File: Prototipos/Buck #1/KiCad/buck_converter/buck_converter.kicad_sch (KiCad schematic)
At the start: 6 parts, among them J1 Screw_Terminal_01x02, J2 Screw_Terminal_01x02, Q2 IRF9540NPBF

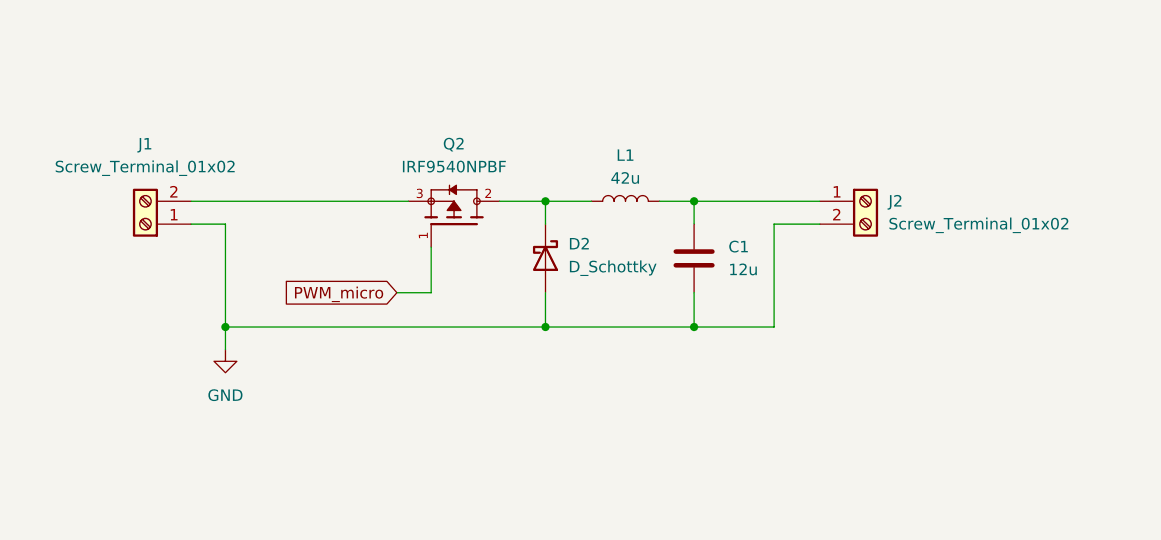
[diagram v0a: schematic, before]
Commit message: Avances circuito KiCad, nuevos calculos para frecuencia más baja
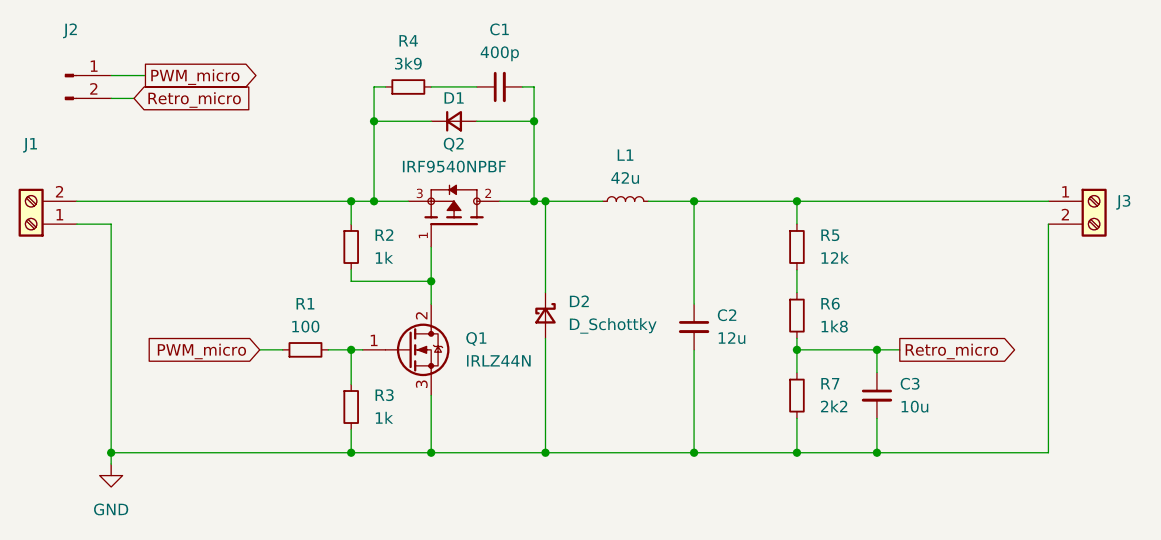
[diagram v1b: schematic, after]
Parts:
- removed C1: 12u, symbol Device:C
- removed D2: D_Schottky, symbol Device:D_Schottky
- removed L1: 42u, symbol Device:L
- added C1: 400p, Capacitor_THT:C_Disc_D3.8mm_W2.6mm_P2.50mm, symbol Device:C_Small
- added C2: 12u, Capacitor_THT:C_Disc_D3.8mm_W2.6mm_P2.50mm, symbol Device:C_Small
- added C3: 10u, Capacitor_THT:C_Disc_D3.8mm_W2.6mm_P2.50mm, symbol Device:C_Small
- added D1: D_Small, Diode_THT:D_A-405_P10.16mm_Horizontal, symbol Device:D_Small
- added D2: D_Schottky, Diode_THT:D_A-405_P10.16mm_Horizontal, symbol Device:D_Schottky_Small
- added J2: Conn_01x02_Pin, Connector_PinHeader_2.54mm:PinHeader_1x02_P2.54mm_Vertical, symbol Connector:Conn_01x02_Pin
- added L1: 42u, Inductor_THT:L_Axial_L16.0mm_D6.3mm_P25.40mm_Horizontal_Fastron_VHBCC, symbol Device:L_Small
- added Q1: IRLZ44N, Package_TO_SOT_THT:TO-220-3_Vertical, symbol Transistor_FET:IRLZ44N
- added R1: 100, Resistor_THT:R_Axial_DIN0207_L6.3mm_D2.5mm_P15.24mm_Horizontal, symbol Device:R_Small
- added R2, R3: 1k, Resistor_THT:R_Axial_DIN0207_L6.3mm_D2.5mm_P15.24mm_Horizontal, symbol Device:R_Small
- added R4: 3k9, Resistor_THT:R_Axial_DIN0207_L6.3mm_D2.5mm_P15.24mm_Horizontal, symbol Device:R_Small
- added R5: 12k, Resistor_THT:R_Axial_DIN0207_L6.3mm_D2.5mm_P15.24mm_Horizontal, symbol Device:R_Small
- added R6: 1k8, Resistor_THT:R_Axial_DIN0207_L6.3mm_D2.5mm_P15.24mm_Horizontal, symbol Device:R_Small
- added R7: 2k2, Resistor_THT:R_Axial_DIN0207_L6.3mm_D2.5mm_P15.24mm_Horizontal, symbol Device:R_Small
- J1: footprint (none) -> TerminalBlock_Phoenix:TerminalBlock_Phoenix_MPT-0,5-2-2.54_1x02_P2.54mm_Horizontal
- J3: renamed from J2; footprint (none) -> TerminalBlock_Phoenix:TerminalBlock_Phoenix_MPT-0,5-2-2.54_1x02_P2.54mm_Horizontal
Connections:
- net GND: now also C2.2, C3.2, D2.2 (A), Q1.3 (S), R3.2, R7.2
- net PWM_micro: now also J2.1 (Pin_1), R1.1; no longer Q2.1
- net at J1.2 (Pin_2), Q2.3: now also D1.1 (K), R2.1, R4.1
- net at Q2.2: now also C1.2, D1.2 (A), D2.1 (K), L1.1
- net at J3.1 (Pin_1): now also C2.1, L1.2, R5.1
- new net: Q1.2 (D), Q2.1, R2.2
- new net: Q1.1 (G), R1.2, R3.1
- new net: C1.1, R4.2
- new net: R5.2, R6.1
- new net Retro_micro: C3.1, J2.2 (Pin_2), R6.2, R7.1
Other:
- moved on the sheet: J1, J3

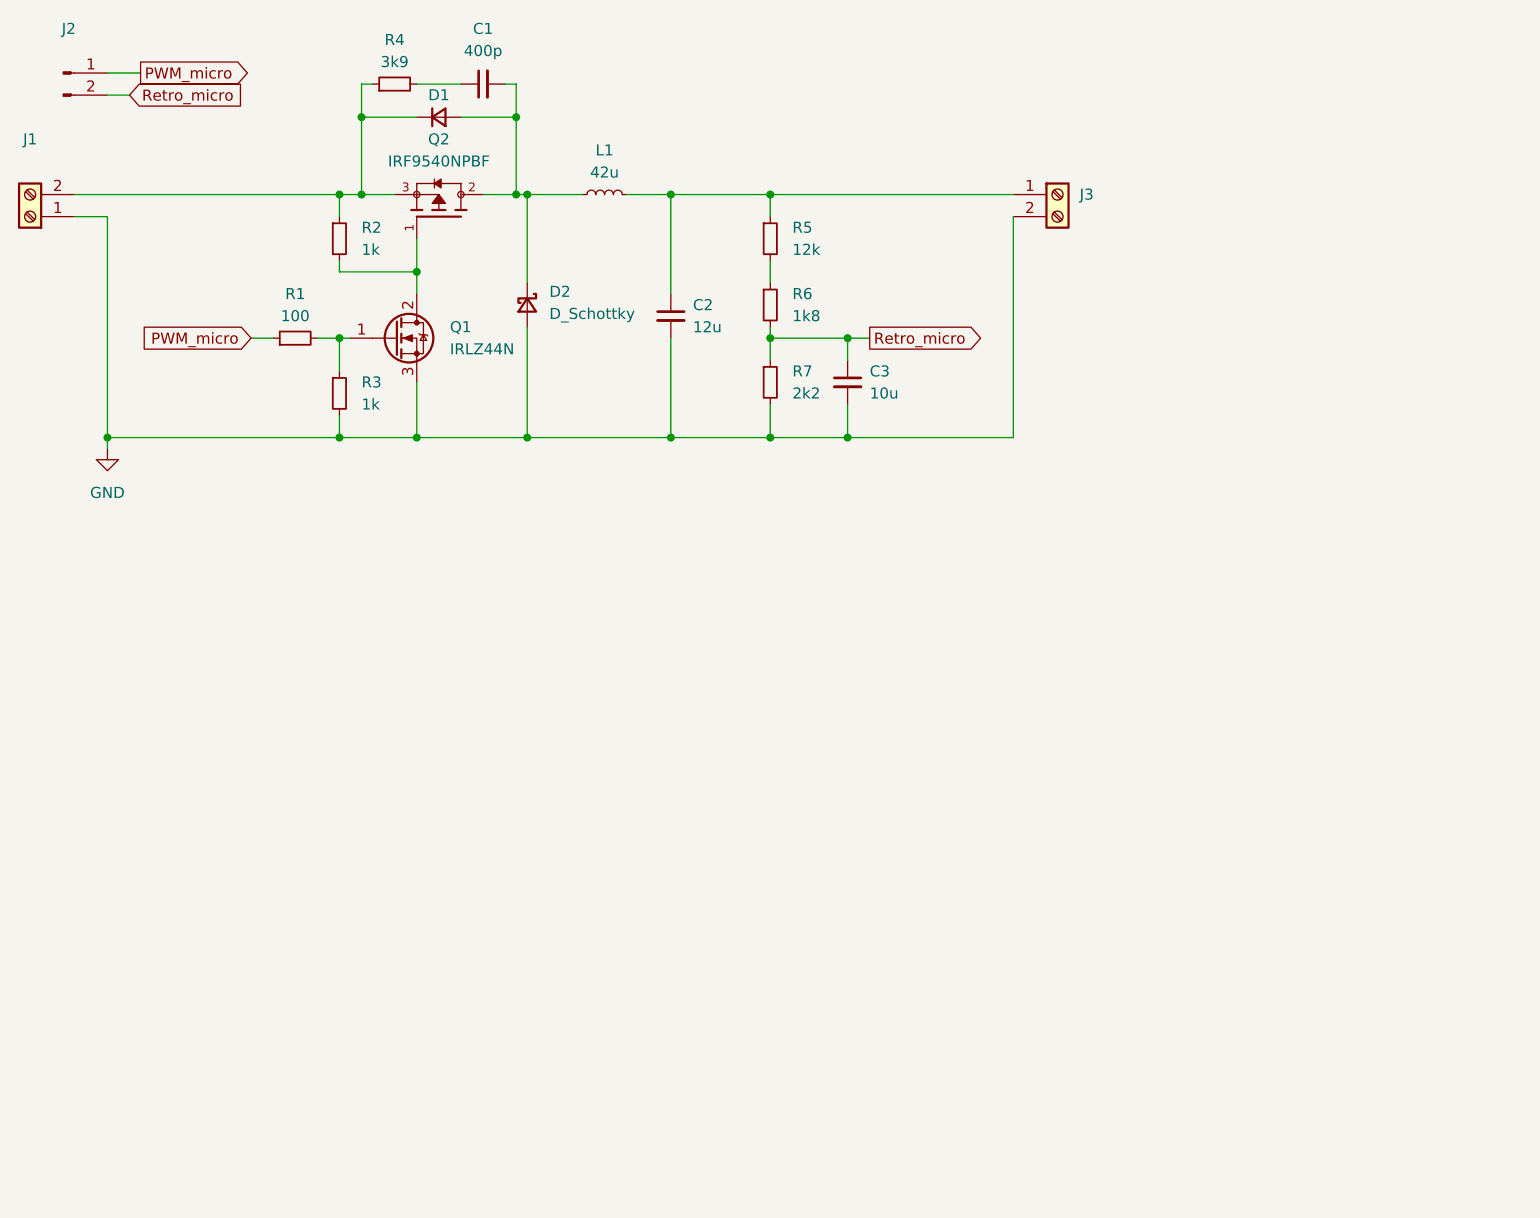
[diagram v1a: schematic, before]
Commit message: Avances diseño del circuito, definición de algunos componentes
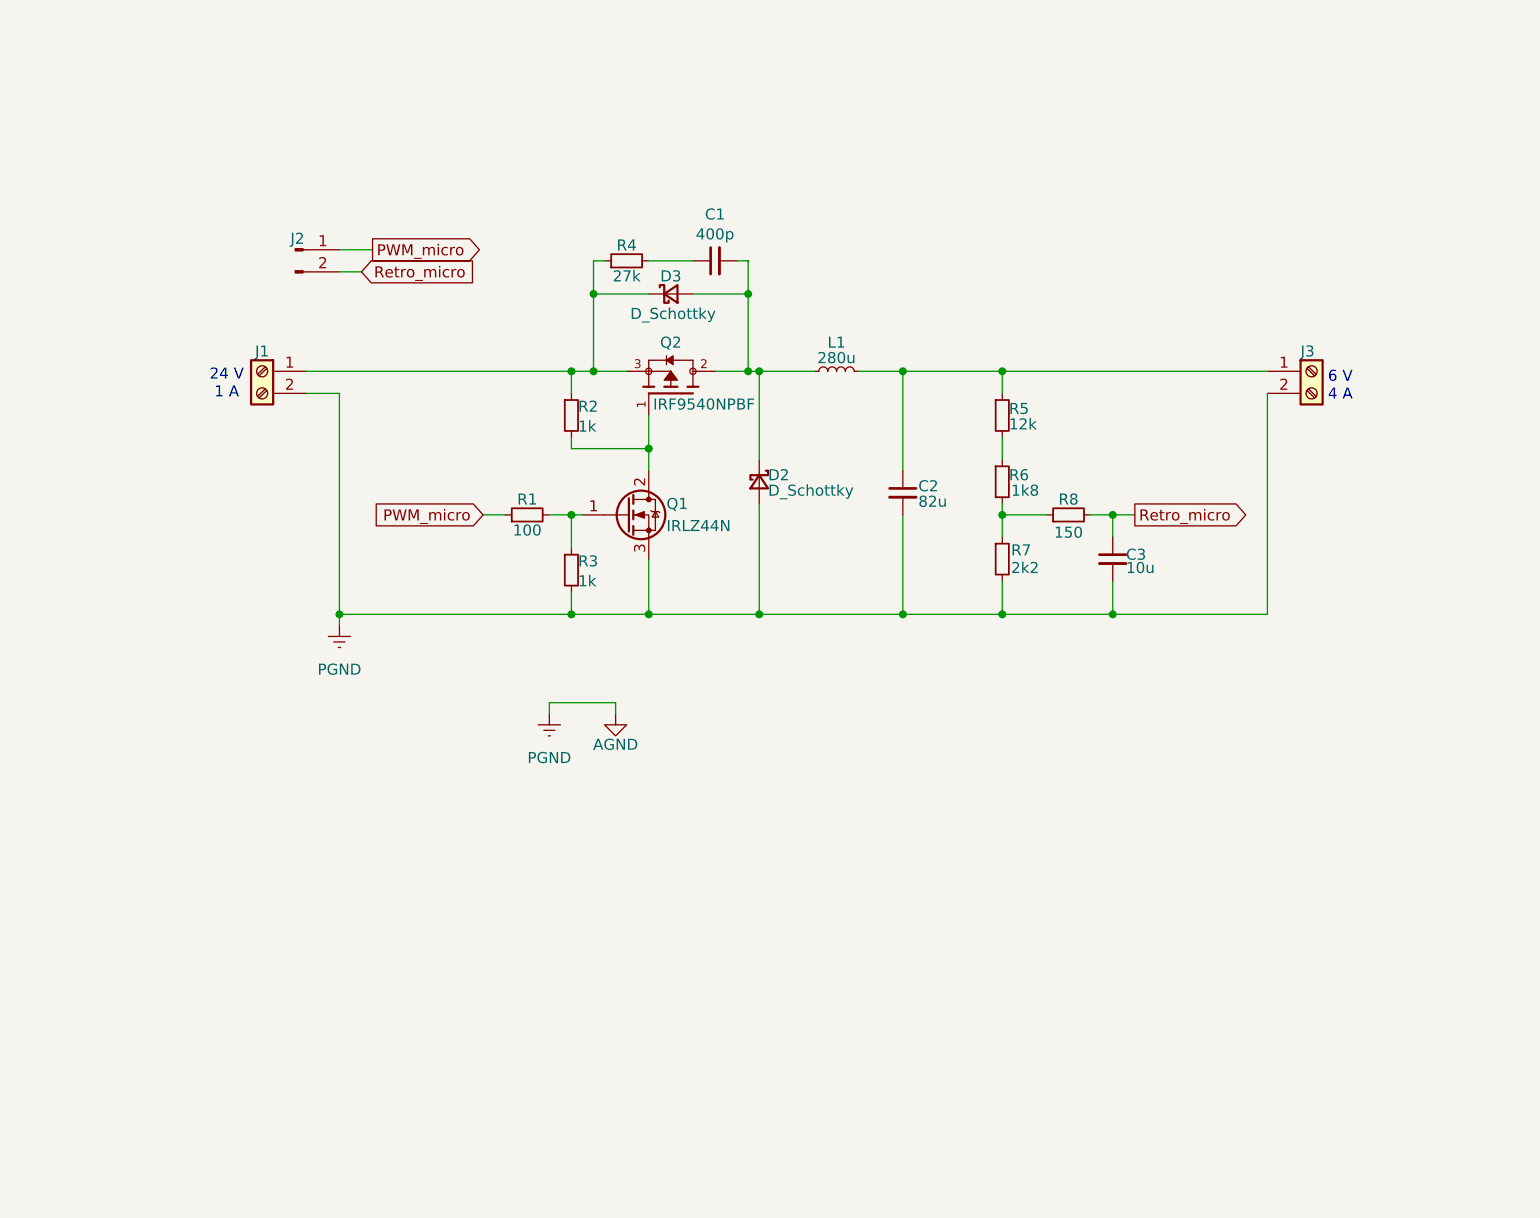
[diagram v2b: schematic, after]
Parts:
- removed D1: D_Small, Diode_THT:D_A-405_P10.16mm_Horizontal, symbol Device:D_Small
- added D3: D_Schottky, Diode_THT:D_A-405_P10.16mm_Horizontal, symbol Device:D_Schottky_Small
- added R8: 150, Resistor_THT:R_Axial_DIN0207_L6.3mm_D2.5mm_P15.24mm_Horizontal, symbol Device:R_Small
- C2: value 12u -> 82u
- L1: value 42u -> 280u
- R4: value 3k9 -> 27k
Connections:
- net Retro_micro: now also R8.2; no longer R6.2, R7.1
- net at Q2.3, R2.1, R4.1: now also J1.1 (Pin_1), D3.1 (K); no longer J1.2 (Pin_2)
- net at C1.2, D2.1 (K), L1.1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: now also D3.2 (A)
- net GND renamed AGND
- net AGND: now also J1.2 (Pin_2); no longer J1.1 (Pin_1)
- new net: R6.2, R7.1, R8.1
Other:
- note added: "24 V 1 A"
- note added: "6 V 4 A"
- company: (none) -> Alesandria - Cignetti - Galliano
- title: (none) -> Prototipo de Convertidor Buck
- moved on the sheet: C1, C2, C3, D2, J1, J2, J3, L1, Q1, Q2, R1, R2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

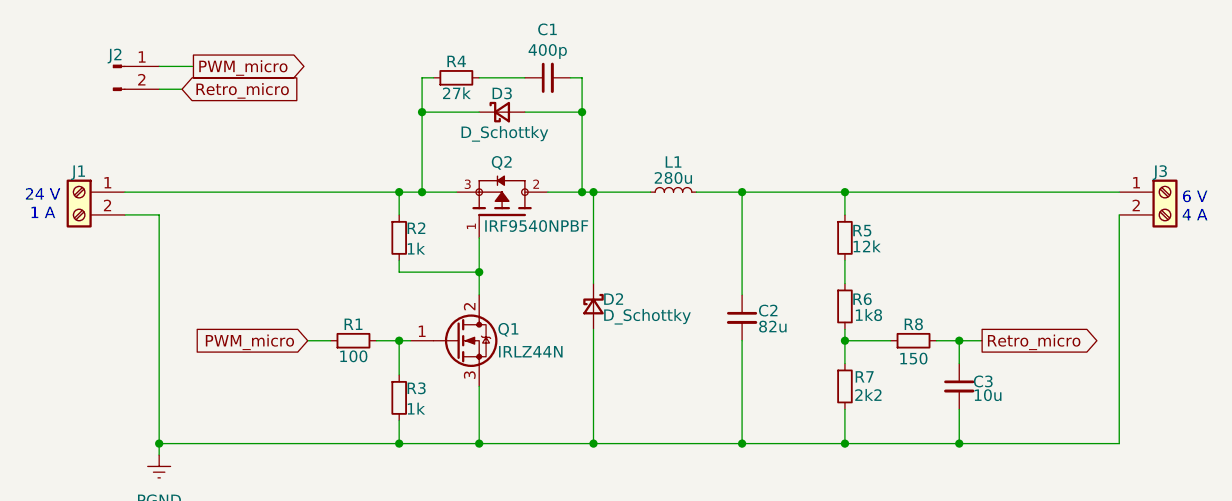
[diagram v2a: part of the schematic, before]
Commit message: Cambio de valores en circuito
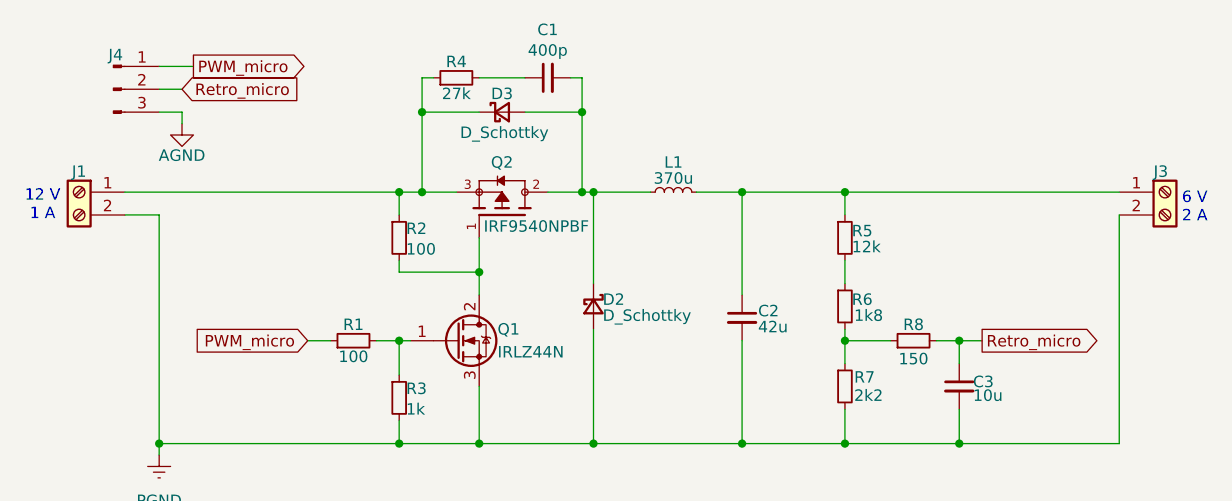
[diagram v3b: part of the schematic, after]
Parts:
- removed J2: Conn_01x02_Pin, Connector_PinHeader_2.54mm:PinHeader_1x02_P2.54mm_Vertical, symbol Connector:Conn_01x02_Pin
- added J4: Conn_01x03_Pin, symbol Connector:Conn_01x03_Pin
- C2: value 82u -> 42u
- L1: value 280u -> 370u
- R2: value 1k -> 100
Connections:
- net AGND: now also J4.3 (Pin_3)
- net PWM_micro: now also J4.1 (Pin_1)
- net Retro_micro: now also J4.2 (Pin_2)
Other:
- note added: "12 V 1 A"
- note added: "6 V 2 A"
- note removed: "24 V 1 A"
- note removed: "6 V 4 A"
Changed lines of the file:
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@@
 		(comment 1 "Componentes calculador para 15 kHz")
 	)
-	(text "6 V\n4 A"
+	(text "6 V\n2 A"
 		(exclude_from_sim no)
 		(at 174.752 55.118 0)
@@
 		)
 	)
-	(text "24 V\n1 A"
+	(text "12 V\n1 A"
 		(exclude_from_sim no)
 		(at 46.736 54.864 0)
@@
 	(wire
 		(pts
+			(xy 59.69 44.45) (xy 62.23 44.45)
+		)
+		(stroke
+			(width 0)
+			(type default)
+		)
+	)
+	(wire
+		(pts
 			(xy 135.89 53.34) (xy 135.89 55.88)
 		)
@@
 		(pts
 			(xy 135.89 69.85) (xy 140.97 69.85)
+		)
+		(stroke
+			(width 0)
+			(type default)
+		)
+	)
+	(wire
+		(pts
+			(xy 62.23 44.45) (xy 62.23 45.72)
 		)
 		(stroke
@@
 			)
 		)
-		(property "Value" "1k"
+		(property "Value" "100"
 			(at 87.122 59.69 0)
 			(effects
@@
 				(path "/bb8bc01e-43dc-40c7-9cc7-76fd3e77d2b7"
 					(reference "R2")
-					(unit 1)
-				)
-			)
-		)
-	)
-	(symbol
-		(lib_id "Connector:Conn_01x02_Pin")
-		(at 54.61 39.37 0)
-		(unit 1)
-		(exclude_from_sim no)
-		(in_bom yes)
-		(on_board yes)
-		(dnp no)
-		(property "Reference" "J2"
-			(at 54.864 38.1 0)
-			(effects
-				(font
-					(size 1.27 1.27)
-				)
-			)
-		)
-		(property "Value" "Conn_01x02_Pin"
-			(at 55.245 36.83 0)
-			(effects
-				(font
-					(size 1.27 1.27)
-				)
-				(hide yes)
-			)
-		)
-		(property "Footprint" "Connector_PinHeader_2.54mm:PinHeader_1x02_P2.54mm_Vertical"
-			(at 54.61 39.37 0)
-			(effects
-				(font
-					(size 1.27 1.27)
-				)
-				(hide yes)
-			)
-		)
-		(property "Datasheet" "~"
-			(at 54.61 39.37 0)
-			(effects
-				(font
-					(size 1.27 1.27)
-				)
-				(hide yes)
-			)
-		)
-		(property "Description" "Generic connector, single row, 01x02, script generated"
-			(at 54.61 39.37 0)
-			(effects
-				(font
-					(size 1.27 1.27)
-				)
-				(hide yes)
-			)
-		)
-		(pin "1"
-		)
-		(pin "2"
-		)
-		(instances
-			(project ""
-				(path "/bb8bc01e-43dc-40c7-9cc7-76fd3e77d2b7"
-					(reference "J2")
 					(unit 1)
 				)
@@
 	)
 	(symbol
+		(lib_id "Connector:Conn_01x03_Pin")
+		(at 54.61 41.91 0)
+		(unit 1)
+		(exclude_from_sim no)
+		(in_bom yes)
+		(on_board yes)
+		(dnp no)
+		(property "Reference" "J4"
+			(at 54.864 38.1 0)
+			(effects
+				(font
+					(size 1.27 1.27)
+				)
+			)
+		)
+		(property "Value" "Conn_01x03_Pin"
+			(at 55.245 36.83 0)
+			(effects
+				(font
+					(size 1.27 1.27)
+				)
+				(hide yes)
+			)
+		)
+		(property "Footprint" ""
+			(at 54.61 41.91 0)
+			(effects
+				(font
+					(size 1.27 1.27)
+				)
+				(hide yes)
+			)
+		)
+		(property "Datasheet" "~"
+			(at 54.61 41.91 0)
+			(effects
+				(font
+					(size 1.27 1.27)
+				)
+				(hide yes)
+			)
+		)
+		(property "Description" "Generic connector, single row, 01x03, script generated"
+			(at 54.61 41.91 0)
+			(effects
+				(font
+					(size 1.27 1.27)
+				)
+				(hide yes)
+			)
+		)
+		(pin "3"
+		)
+		(pin "1"
+		)
+		(pin "2"
+		)
+		(instances
+			(project ""
+				(path "/bb8bc01e-43dc-40c7-9cc7-76fd3e77d2b7"
+					(reference "J4")
+					(unit 1)
+				)
+			)
+		)
+	)
+	(symbol
 		(lib_id "power:GND")
 		(at 91.44 92.71 0)
@@
 			)
 		)
-		(property "Value" "82u"
+		(property "Value" "42u"
 			(at 126.238 68.326 0)
 			(effects
@@
 	)
 	(symbol
+		(lib_id "power:GND")
+		(at 62.23 45.72 0)
+		(unit 1)
+		(exclude_from_sim no)
+		(in_bom yes)
+		(on_board yes)
+		(dnp no)
+		(property "Reference" "#PWR04"
+			(at 62.23 52.07 0)
+			(effects
+				(font
+					(size 1.27 1.27)
+				)
+				(hide yes)
+			)
+		)
+		(property "Value" "AGND"
+			(at 62.23 49.276 0)
+			(effects
+				(font
+					(size 1.27 1.27)
+				)
+			)
+		)
+		(property "Footprint" ""
+			(at 62.23 45.72 0)
+			(effects
+				(font
+					(size 1.27 1.27)
+				)
+				(hide yes)
+			)
+		)
+		(property "Datasheet" ""
+			(at 62.23 45.72 0)
+			(effects
+				(font
+					(size 1.27 1.27)
+				)
+				(hide yes)
+			)
+		)
+		(property "Description" "Power symbol creates a global label with name \"GND\" , ground"
+			(at 62.23 45.72 0)
+			(effects
+				(font
+					(size 1.27 1.27)
+				)
+				(hide yes)
+			)
+		)
+		(pin "1"
+		)
+		(instances
+			(project "buck_converter"
+				(path "/bb8bc01e-43dc-40c7-9cc7-76fd3e77d2b7"
+					(reference "#PWR04")
+					(unit 1)
+				)
+			)
+		)
+	)
+	(symbol
 		(lib_id "Device:C_Small")
 		(at 102.87 40.64 90)
@@
 			)
 		)
-		(property "Value" "280u"
+		(property "Value" "370u"
 			(at 116.84 51.816 90)
 			(effects
